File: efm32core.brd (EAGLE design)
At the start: 52.1 x 53.3 mm, 66 parts, among them Q1 MMBT5088, U3 USD-SOCKETNEW, X1 48.0MHz, Y1 32.768kHz

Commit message: do some line ups
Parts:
- moved L2 4.19 mm to (15.9, 7.49)
- moved IP4220CZ6 0.57 mm to (9.40, 8.89)
- moved R6 0.13 mm to (22.1, 7.49)
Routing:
- net USB_DP: track 0.00 -> 52.9 mm, vias 0 -> 1
- net USB_DM: track 0.00 -> 46.9 mm, vias 0 -> 1
- net RESET: track 0.00 -> 46.0 mm, vias 0 -> 1
- net USB_ID: track 3.37 -> 43.7 mm, vias 0 -> 1
- net 3.3V: track 56.4 -> 75.5 mm
- net LFXTAL_N: track 0.00 -> 9.20 mm
- net VDD: track 31.8 -> 40.4 mm
- net N$4: track 0.00 -> 8.59 mm, vias 0 -> 2
- net M_USB_DM: track 0.00 -> 7.91 mm, vias 0 -> 1
- net N$6: track 0.00 -> 6.33 mm
- net M_USB_DP: track 0.00 -> 5.92 mm, vias 0 -> 1
- net LFXTAL_P: track 0.00 -> 5.78 mm
- net N$14: track 6.45 -> 11.8 mm, vias 0 -> 2
- net N$8: track 0.00 -> 5.23 mm
- net M_USB_ID: track 0.00 -> 5.05 mm, vias 0 -> 1
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
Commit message: add polygon
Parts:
- moved R3 2.03 mm to (6.35, 6.35)
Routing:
- net N$13: track 10.0 -> 11.5 mm
- net USB_DP: track 52.9 -> 54.3 mm
- net GND: vias 0 -> 4
- added copper zone on layer 1, net GND
- added copper zone on layer 16, net GND
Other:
- outline, holes or cut-outs redrawn

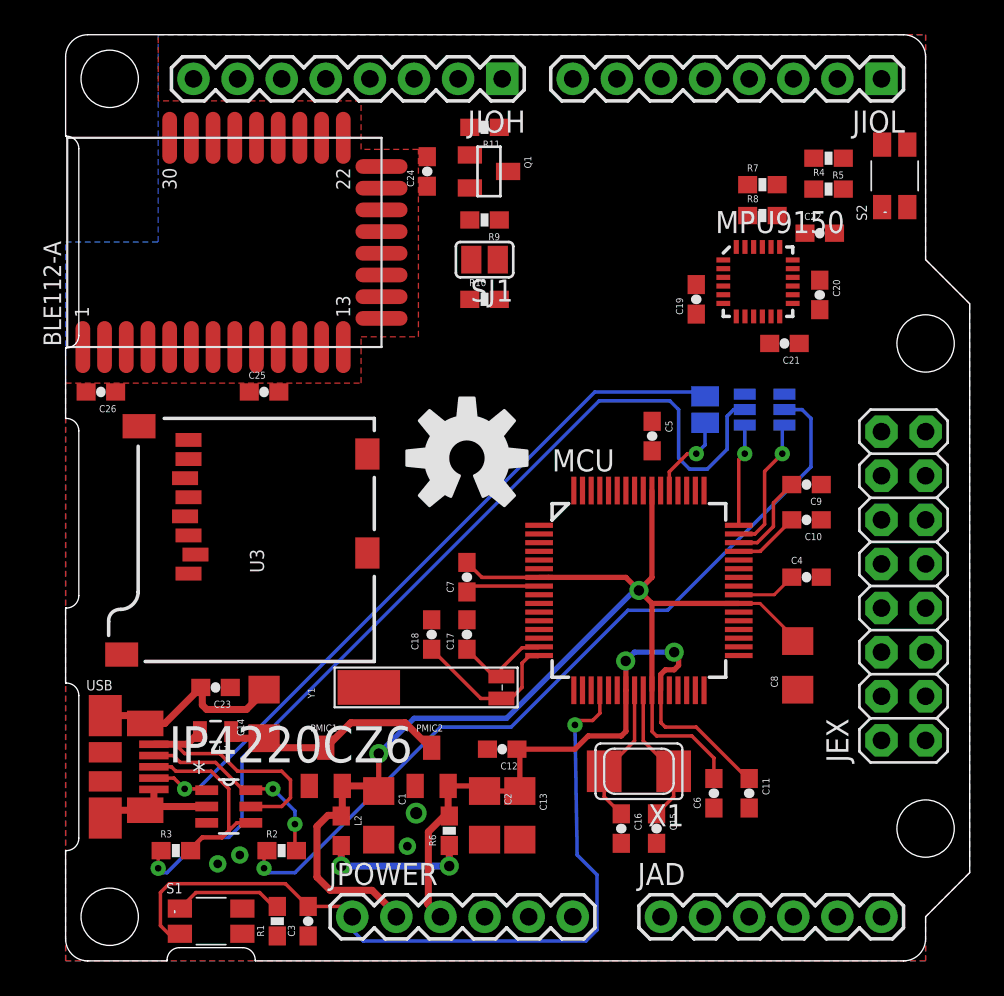
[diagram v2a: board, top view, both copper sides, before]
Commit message: connect some routes
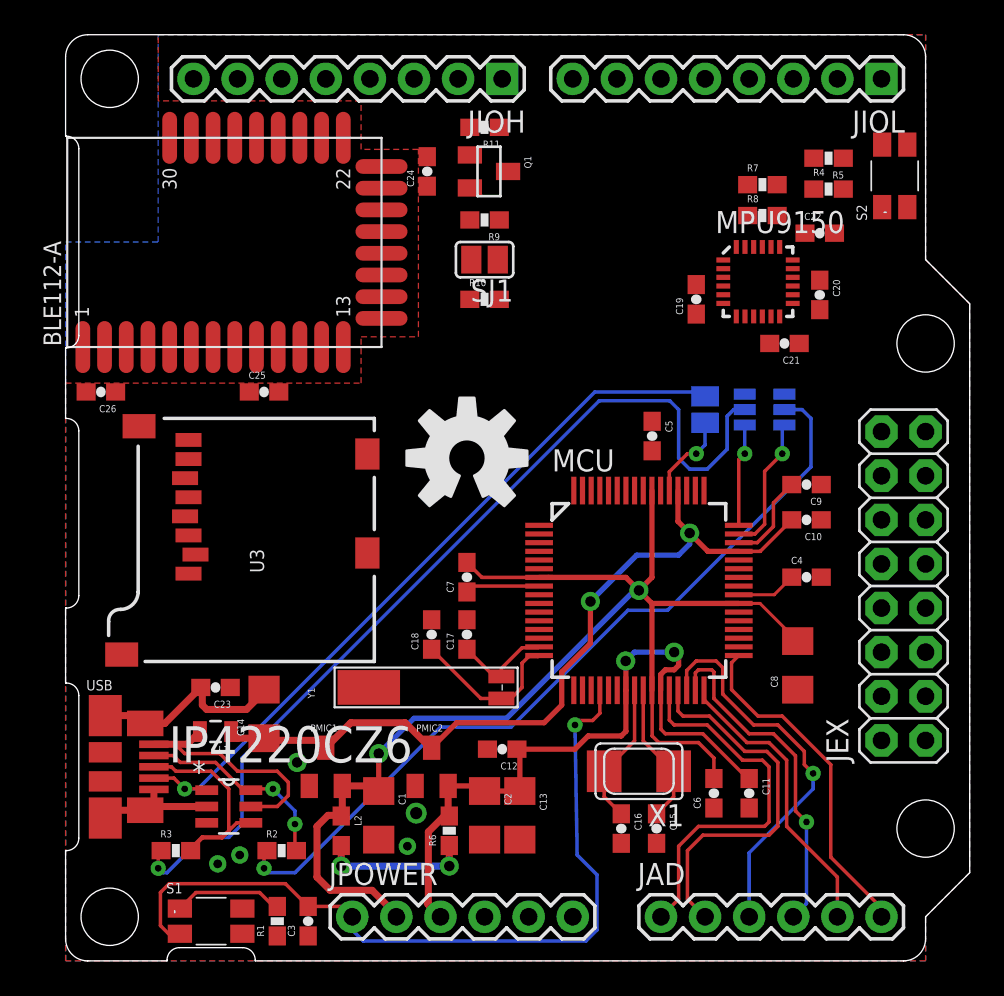
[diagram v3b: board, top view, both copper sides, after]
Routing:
- net 5V: track 16.9 -> 47.9 mm, vias 0 -> 2
- net ADCH2: track 0.00 -> 22.4 mm, vias 0 -> 1
- net ADCH0: track 0.00 -> 22.0 mm
- net ADCH1: track 0.00 -> 21.9 mm
- net ADCH3: track 0.00 -> 19.6 mm, vias 0 -> 1
- net ADCH5: track 0.00 -> 19.6 mm
- net ADCH4: track 0.00 -> 17.0 mm
- net GND: vias 4 -> 5

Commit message: route
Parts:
- moved C18 3.47 mm to (17.7, 18.3), turned to 180 degrees
- moved C7 2.16 mm to (24.1, 24.0), turned to 0 degrees
- moved C17 2.04 mm to (21.1, 18.7)
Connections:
- removed net VIN: JPOWER.6
- new net N$5: U3.CD1
- net 5V: now also JPOWER.6
- net GND: now also JIOH.7, U3.CD2, U3.GND1, U3.GND3
- net US1_RX: now also BLE112-A.P0_3
- net US1_TX: now also BLE112-A.P0_2
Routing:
- net US2_RX: track 0.00 -> 25.8 mm
- net US2_CLK: track 0.00 -> 24.4 mm
- net 3.3V: track 75.6 -> 98.5 mm, vias 2 -> 4
- net US2_TX: track 0.00 -> 22.0 mm, vias 0 -> 2
- net US2_CS: track 0.00 -> 21.8 mm
- net 5V: track 47.9 -> 65.7 mm, vias 2 -> 3
- net US1_TX: track 0.00 -> 15.5 mm
- net US1_RX: track 0.00 -> 15.5 mm
- net GND: track 23.6 -> 19.5 mm
- net LFXTAL_N: track 9.20 -> 11.9 mm
- net LFXTAL_P: track 5.78 -> 7.76 mm

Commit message: route accel
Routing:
- net 3.3V: track 98.5 -> 176.6 mm, vias 4 -> 7
- net PA2: track 0.00 -> 52.2 mm
- net I2C0_SDA: track 0.00 -> 41.5 mm
- net I2C0_SCL: track 0.00 -> 40.7 mm, vias 0 -> 2
- net N$9: track 0.00 -> 5.70 mm
- net GND: track 19.5 -> 24.3 mm, vias 5 -> 6
- net N$15: track 0.00 -> 2.67 mm
- net N$12: track 0.00 -> 1.73 mm
- net USB_DP: track 54.3 -> 53.4 mm

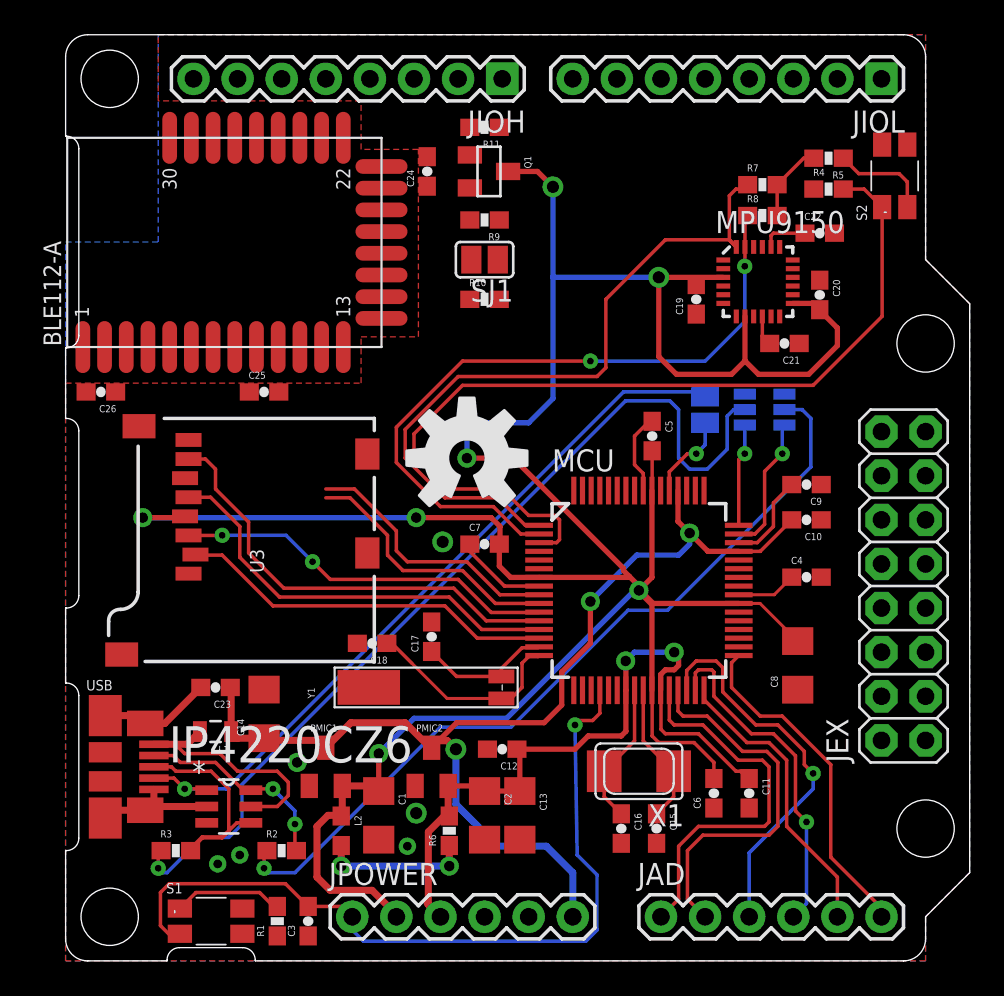
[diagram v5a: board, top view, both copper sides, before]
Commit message: optimize some routes
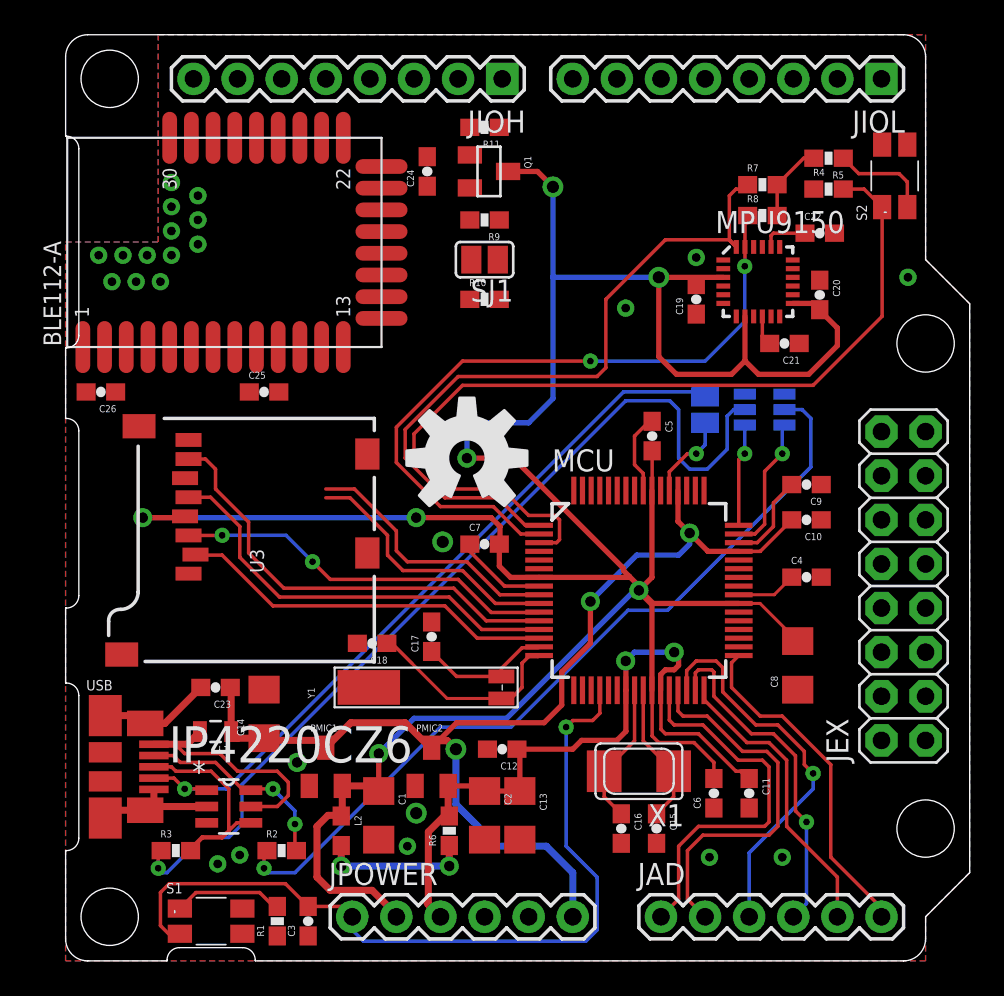
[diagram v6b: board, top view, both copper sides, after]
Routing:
- net RESET: track 46.0 -> 46.7 mm
- net GND: vias 6 -> 24
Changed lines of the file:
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@@
 <wire x1="26.162" y1="9.782" x2="26.162" y2="12.026" width="0.3048" layer="1"/>
 <wire x1="26.162" y1="12.026" x2="25.996" y2="12.192" width="0.3048" layer="1"/>
-<wire x1="25.996" y1="12.192" x2="29.337" y2="12.192" width="0.3048" layer="1"/>
-<wire x1="29.337" y1="12.192" x2="30.099" y2="12.954" width="0.3048" layer="1"/>
-<wire x1="30.099" y1="12.954" x2="32.004" y2="12.954" width="0.3048" layer="1"/>
-<wire x1="32.004" y1="12.954" x2="32.27" y2="13.22" width="0.3048" layer="1"/>
+<wire x1="25.996" y1="12.192" x2="29.21" y2="12.192" width="0.3048" layer="1"/>
+<wire x1="29.21" y1="12.192" x2="29.718" y2="12.7" width="0.3048" layer="1"/>
+<wire x1="29.718" y1="12.7" x2="31.75" y2="12.7" width="0.3048" layer="1"/>
+<wire x1="31.75" y1="12.7" x2="32.27" y2="13.22" width="0.3048" layer="1"/>
 <wire x1="32.27" y1="13.22" x2="32.27" y2="15.586" width="0.3048" layer="1"/>
 <wire x1="36.449" y1="13.081" x2="34.544" y2="13.081" width="0.2032" layer="1"/>
@@
 <via x="20.193" y="8.509" extent="1-16" drill="0.7"/>
 <via x="19.685" y="6.604" extent="1-16" drill="0.5"/>
-<polygon width="0.254" layer="16" spacing="0.254" pour="cutout" isolate="0.4064">
+<polygon width="0.254" layer="16" spacing="0.254" isolate="0.4064">
 <vertex x="5.334" y="53.34"/>
 <vertex x="49.53" y="53.34"/>
@@
 <via x="10.033" y="6.096" extent="1-16" drill="0.5"/>
 <via x="13.335" y="11.43" extent="1-16" drill="0.6"/>
-<polygon width="0.254" layer="1" spacing="0.254" pour="cutout" isolate="0.4064">
+<polygon width="0.254" layer="1" spacing="0.254" isolate="0.4064">
 <vertex x="5.334" y="53.34"/>
 <vertex x="49.53" y="53.34"/>
@@
 <vertex x="49.53" y="0"/>
 <vertex x="0" y="0"/>
-<vertex x="0" y="33.274"/>
-<vertex x="17.018" y="33.274"/>
-<vertex x="17.018" y="35.941"/>
-<vertex x="20.32" y="35.941"/>
-<vertex x="20.32" y="46.736"/>
-<vertex x="17.018" y="46.736"/>
-<vertex x="17.018" y="49.53"/>
-<vertex x="5.334" y="49.53"/>
+<vertex x="0" y="41.402"/>
+<vertex x="5.334" y="41.402"/>
 </polygon>
 <contactref element="JIOH" pad="7"/>
@@
 <wire x1="32.766" y1="30.226" x2="33.616" y2="31.076" width="0.2032" layer="1"/>
 <wire x1="33.616" y1="31.076" x2="33.782" y2="31.076" width="0.2032" layer="1"/>
-<wire x1="43.434" y1="39.204" x2="44.284" y2="41.91" width="0" layer="19" extent="1-1"/>
-<wire x1="41.878" y1="38.866" x2="43.434" y2="39.204" width="0" layer="19" extent="1-1"/>
-<wire x1="41.878" y1="39.866" x2="41.878" y2="38.866" width="0" layer="19" extent="1-1"/>
-<wire x1="41.878" y1="40.366" x2="41.878" y2="39.866" width="0" layer="19" extent="1-1"/>
+<via x="4.699" y="40.64" extent="1-16" drill="0.5"/>
+<via x="3.302" y="40.64" extent="1-16" drill="0.5"/>
+<via x="1.905" y="40.64" extent="1-16" drill="0.5"/>
+<via x="4.064" y="39.116" extent="1-16" drill="0.5"/>
+<via x="2.667" y="39.116" extent="1-16" drill="0.5"/>
+<via x="6.096" y="42.037" extent="1-16" drill="0.5"/>
+<via x="6.096" y="43.434" extent="1-16" drill="0.5"/>
+<via x="6.096" y="44.831" extent="1-16" drill="0.5"/>
+<via x="7.62" y="44.069" extent="1-16" drill="0.5"/>
+<via x="7.62" y="42.672" extent="1-16" drill="0.5"/>
+<via x="6.096" y="40.64" extent="1-16" drill="0.5"/>
+<via x="7.62" y="41.275" extent="1-16" drill="0.5"/>
+<via x="5.461" y="39.116" extent="1-16" drill="0.5"/>
+<via x="37.084" y="5.969" extent="1-16" drill="0.5"/>
+<via x="41.275" y="5.969" extent="1-16" drill="0.5"/>
+<via x="48.514" y="39.37" extent="1-16" drill="0.5"/>
+<via x="36.322" y="40.513" extent="1-16" drill="0.5"/>
+<via x="32.258" y="37.592" extent="1-16" drill="0.5"/>
+<wire x1="41.878" y1="39.866" x2="41.878" y2="40.366" width="0" layer="19" extent="1-1"/>
+<wire x1="41.878" y1="38.866" x2="41.878" y2="39.866" width="0" layer="19" extent="1-1"/>
+<wire x1="43.434" y1="39.204" x2="41.878" y2="38.866" width="0" layer="19" extent="1-1"/>
 <wire x1="42.252" y1="35.56" x2="41.878" y2="38.866" width="0" layer="19" extent="1-1"/>
-<wire x1="36.322" y1="37.25" x2="41.878" y2="38.866" width="0" layer="19" extent="1-1"/>
-<wire x1="33.782" y1="31.076" x2="36.322" y2="37.25" width="0" layer="19" extent="1-1"/>
-<wire x1="27.27" y1="21.586" x2="33.27" y2="27.086" width="0" layer="19" extent="1-1"/>
-<wire x1="21.717" y1="24.13" x2="23.28" y2="24.003" width="0" layer="19" extent="1-1"/>
-<wire x1="17.38" y1="23.492" x2="21.717" y2="24.13" width="0" layer="19" extent="1-1"/>
-<wire x1="21.082" y1="19.519" x2="23.28" y2="23.583" width="0" layer="19" extent="1-1"/>
-<wire x1="16.803" y1="18.288" x2="21.082" y2="19.519" width="0" layer="19" extent="1-1"/>
-<wire x1="11.43" y1="15.624" x2="16.803" y2="18.288" width="0" layer="19" extent="1-1"/>
-<wire x1="7.874" y1="15.66" x2="11.43" y2="15.624" width="0" layer="19" extent="1-1"/>
-<wire x1="3.23" y1="17.642" x2="4.136" y2="14.126" width="0" layer="19" extent="1-1"/>
-<wire x1="5.086" y1="9.876" x2="4.586" y2="13.676" width="0" layer="19" extent="1-1"/>
-<wire x1="8.763" y1="5.588" x2="8.128" y2="8.89" width="0" layer="19" extent="1-1"/>
-<wire x1="10.033" y1="6.096" x2="8.763" y2="5.588" width="0" layer="19" extent="1-1"/>
-<wire x1="13.335" y1="11.43" x2="11.43" y2="15.494" width="0" layer="19" extent="1-1"/>
-<wire x1="14.036" y1="10.076" x2="13.335" y2="11.43" width="0" layer="19" extent="1-1"/>
-<wire x1="18.034" y1="6.982" x2="14.036" y2="10.076" width="0" layer="19" extent="1-1"/>
-<wire x1="19.685" y1="6.604" x2="18.034" y2="6.982" width="0" layer="19" extent="1-1"/>
-<wire x1="20.193" y1="8.509" x2="19.685" y2="6.604" width="0" layer="19" extent="1-1"/>
-<wire x1="20.132" y1="10.076" x2="20.193" y2="8.509" width="0" layer="19" extent="1-1"/>
-<wire x1="24.13" y1="6.982" x2="20.193" y2="8.509" width="0" layer="19" extent="1-1"/>
-<wire x1="26.162" y1="6.982" x2="24.13" y2="6.982" width="0" layer="19" extent="1-1"/>
-<wire x1="24.13" y1="2.54" x2="24.13" y2="6.982" width="0" layer="19" extent="1-1"/>
-<wire x1="26.67" y1="2.54" x2="24.13" y2="2.54" width="0" layer="19" extent="1-1"/>
+<wire x1="48.514" y1="39.37" x2="44.284" y2="41.91" width="0" layer="19" extent="1-1"/>
+<wire x1="37.338" y1="8.802" x2="37.084" y2="5.969" width="0" layer="19" extent="1-1"/>
+<wire x1="36.322" y1="37.25" x2="36.322" y2="40.513" width="0" layer="19" extent="1-1"/>
+<wire x1="8.128" y1="8.89" x2="8.763" y2="5.588" width="0" layer="19" extent="1-1"/>
 <wire x1="24.296" y1="12.192" x2="20.132" y2="10.076" width="0" layer="19" extent="1-1"/>
-<wire x1="12.192" y1="1.436" x2="10.033" y2="6.096" width="0" layer="19" extent="1-1"/>
-<wire x1="13.97" y1="1.436" x2="12.192" y2="1.436" width="0" layer="19" extent="1-1"/>
-<wire x1="32.004" y1="6.77" x2="26.162" y2="6.982" width="0" layer="19" extent="1-1"/>
-<wire x1="34.036" y1="6.77" x2="32.004" y2="6.77" width="0" layer="19" extent="1-1"/>
-<wire x1="37.338" y1="8.802" x2="34.036" y2="6.77" width="0" layer="19" extent="1-1"/>
-<wire x1="39.37" y1="8.802" x2="37.338" y2="8.802" width="0" layer="19" extent="1-1"/>
-<wire x1="42.164" y1="15.618" x2="39.37" y2="8.802" width="0" layer="19" extent="1-1"/>
-<wire x1="43.522" y1="22.098" x2="42.164" y2="15.618" width="0" layer="19" extent="1-1"/>
-<wire x1="43.522" y1="25.4" x2="43.522" y2="22.098" width="0" layer="19" extent="1-1"/>
-<wire x1="43.522" y1="27.432" x2="43.522" y2="25.4" width="0" layer="19" extent="1-1"/>
 <wire x1="31.77" y1="15.586" x2="27.27" y2="21.586" width="0" layer="19" extent="1-1"/>
-<wire x1="12.28" y1="32.766" x2="17.38" y2="23.492" width="0" layer="19" extent="1-1"/>
-<wire x1="12.244" y1="35.352" x2="12.28" y2="32.766" width="0" layer="19" extent="1-1"/>
-<wire x1="6.88" y1="27.802" x2="12.28" y2="32.766" width="0" layer="19" extent="1-1"/>
-<wire x1="4.23" y1="30.792" x2="6.88" y2="27.802" width="0" layer="19" extent="1-1"/>
-<wire x1="1.182" y1="32.766" x2="4.23" y2="30.792" width="0" layer="19" extent="1-1"/>
-<wire x1="0.994" y1="35.352" x2="1.182" y2="32.766" width="0" layer="19" extent="1-1"/>
-<wire x1="18.194" y1="45.752" x2="12.244" y2="35.352" width="0" layer="19" extent="1-1"/>
-<wire x1="20.828" y1="46.316" x2="18.194" y2="45.752" width="0" layer="19" extent="1-1"/>
-<wire x1="23.368" y1="40.386" x2="20.828" y2="46.316" width="0" layer="19" extent="1-1"/>
-<wire x1="9.906" y1="50.8" x2="18.194" y2="45.752" width="0" layer="19" extent="1-1"/>
-<wire x1="5.994" y1="47.402" x2="9.906" y2="50.8" width="0" layer="19" extent="1-1"/>
-<wire x1="43.092" y1="44.45" x2="44.284" y2="41.91" width="0" layer="19" extent="1-1"/>
 </signal>
 <signal name="5V">
@@
 <wire x1="17.145" y1="1.143" x2="29.972" y2="1.143" width="0.2032" layer="16"/>
 <wire x1="29.972" y1="1.143" x2="30.607" y2="1.778" width="0.2032" layer="16"/>
-<wire x1="30.607" y1="1.778" x2="30.607" y2="4.953" width="0.2032" layer="16"/>
-<wire x1="30.607" y1="4.953" x2="29.464" y2="6.096" width="0.2032" layer="16"/>
-<wire x1="29.464" y1="6.096" x2="29.337" y2="13.589" width="0.2032" layer="16"/>
-<via x="29.337" y="13.589" extent="1-16" drill="0.381"/>
-<wire x1="29.337" y1="13.589" x2="29.591" y2="13.843" width="0.2032" layer="1"/>
-<wire x1="29.591" y1="13.843" x2="30.353" y2="13.843" width="0.2032" layer="1"/>
+<wire x1="30.607" y1="1.778" x2="30.607" y2="4.826" width="0.2032" layer="16"/>
+<wire x1="30.607" y1="4.826" x2="28.829" y2="6.604" width="0.2032" layer="16"/>
+<wire x1="28.829" y1="6.604" x2="28.829" y2="13.462" width="0.2032" layer="16"/>
+<via x="28.829" y="13.462" extent="1-16" drill="0.381"/>
+<wire x1="28.829" y1="13.462" x2="29.21" y2="13.843" width="0.2032" layer="1"/>
+<wire x1="29.21" y1="13.843" x2="30.353" y2="13.843" width="0.2032" layer="1"/>
 <wire x1="30.353" y1="13.843" x2="30.77" y2="14.26" width="0.2032" layer="1"/>
 <wire x1="30.77" y1="14.26" x2="30.77" y2="15.586" width="0.2032" layer="1"/>

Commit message: optimize
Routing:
- net USB_DM: track 46.9 -> 62.2 mm
- net 3.3V: track 176.6 -> 187.6 mm
- net USB_ID: track 43.7 -> 46.7 mm
- net USB_DP: track 53.4 -> 56.3 mm
- net GND: track 24.3 -> 26.4 mm, vias 24 -> 34
- net VDD: track 40.9 -> 42.4 mm
- net 5V: track 65.7 -> 66.2 mm
